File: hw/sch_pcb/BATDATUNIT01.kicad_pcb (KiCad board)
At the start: 2 copper layers, 136.2 x 85.9 mm, 221 parts, among them J1 USBC_USB4105-GF-A, J2 SD_Card-FPS009-4200-0, J3 HEADER_2x03, J4 46436-9327, Q1 BC817-25, Q2 BC817-25, Q3 BC817-25, Q4 BC817-25, Q5 BC817-25, Q6 BC817-25, Q7 BSS83P, SW1 SKRTLAE010, SW2 KMT031, SW3 SKRTLAE010, SW4 KMT031, U1 MAX14502AETL+, U10 PCF85263A, U11 TCA4307, U12 BQ34Z100, U13 BQ25628E, U14 SN74HC164P, U15 TPS631000DRLR, U16 TPS631000DRLR, U17 TPS631000DRLR, U18 TPS22965-Q1, U2 USBLC6-2SC6, U4 PCA9541ABS/01, U5 AT24CS64-SSHM, U6 SHT35-DIS, U7 TMUX1574DYYR, U8 ATMEGA1284P-AU, U9 MS561101BA03-50, Y1 19.2 MHz, Y2 8 MHz, Y3 ABS07-120-32.768KHZ-T

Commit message: Resolve majority of DRC issues.
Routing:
- net GND: track 91.3 -> 94.1 mm, vias 162 -> 163
- net +3.3V: track 564.8 -> 566.3 mm

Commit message: Change oscillator footprint. WIP
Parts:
- Y1: footprint Crystal:Crystal_SMD_2016-4Pin_2.0x1.6mm -> Crystal:Crystal_SMD_2520-4Pin_2.5x2.0mm
- moved R4 0.51 mm to (189.0, 94.5)
- moved R3 0.34 mm to (186.1, 94.7)
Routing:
- net Net-(C49-Pad1): track 7.74 -> 1.91 mm
- net /FREF: track 10.6 -> 10.00 mm
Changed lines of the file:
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@@
   )
   (footprint "Resistor_SMD:R_0805_2012Metric" (layer "B.Cu")
-    (at 188.55 94.3 90)
+    (at 189.0268 94.488 90)
     (descr "Resistor SMD 0805 (2012 Metric), square (rectangular) end terminal, IPC_7351 nominal, (Body size source: IPC-SM-782 page 72, https://www.pcb-3d.com/wordpress/wp-content/uploads/ipc-sm-782a_amendment_1_and_2.pdf), generated with kicad-footprint-generator")
     (tags "resistor")
@@
   )
   (footprint "Resistor_SMD:R_0805_2012Metric" (layer "B.Cu")
-    (at 185.85 94.5 180)
+    (at 186.1058 94.7166 180)
     (descr "Resistor SMD 0805 (2012 Metric), square (rectangular) end terminal, IPC_7351 nominal, (Body size source: IPC-SM-782 page 72, https://www.pcb-3d.com/wordpress/wp-content/uploads/ipc-sm-782a_amendment_1_and_2.pdf), generated with kicad-footprint-generator")
     (tags "resistor")
@@
     )
   )
-  (footprint "Crystal:Crystal_SMD_2016-4Pin_2.0x1.6mm" (layer "B.Cu")
+  (footprint "Crystal:Crystal_SMD_2520-4Pin_2.5x2.0mm" (layer "B.Cu")
     (at 186.1 92.2)
-    (descr "SMD Crystal SERIES SMD2016/4 http://www.q-crystal.com/upload/5/2015552223166229.pdf, 2.0x1.6mm^2 package")
+    (descr "SMD Crystal SERIES SMD2520/4 http://www.newxtal.com/UploadFiles/Images/2012-11-12-09-29-09-776.pdf, 2.5x2.0mm^2 package")
     (tags "SMD SMT crystal")
     (property "Sheetfile" "BATDATUNIT01.kicad_sch")
@@
     (property "ki_keywords" "Crystal Clock Oscillator")
     (attr smd)
-    (fp_text reference "Y1" (at 2.05 -1.35) (layer "B.SilkS")
-        (effects (font (size 0.8 0.8) (thickness 0.1)) (justify mirror))
+    (fp_text reference "Y1" (at 0 2.2 180) (layer "B.SilkS")
+        (effects (font (size 1 1) (thickness 0.15)) (justify mirror))
     )
-    (fp_text value "19.2 MHz" (at 0 -2) (layer "B.Fab")
+    (fp_text value "19.2 MHz" (at 0 -2.2 180) (layer "B.Fab")
         (effects (font (size 1 1) (thickness 0.15)) (justify mirror))
     )
-    (fp_text user "${REFERENCE}" (at 0 0) (layer "B.Fab")
-        (effects (font (size 0.5 0.5) (thickness 0.075)) (justify mirror))
+    (fp_text user "${REFERENCE}" (at 0 0 180) (layer "B.Fab")
+        (effects (font (size 0.6 0.6) (thickness 0.09)) (justify mirror))
     )
-    (fp_line (start -1.35 -1.15) (end 1.35 -1.15)
+    (fp_line (start -1.65 -1.4) (end 1.65 -1.4)
       (stroke (width 0.12) (type solid)) (layer "B.SilkS"))
-    (fp_line (start -1.35 1.15) (end -1.35 -1.15)
+    (fp_line (start -1.65 1.4) (end -1.65 -1.4)
       (stroke (width 0.12) (type solid)) (layer "B.SilkS"))
-    (fp_line (start -1.4 -1.3) (end 1.4 -1.3)
+    (fp_line (start -1.7 -1.5) (end 1.7 -1.5)
       (stroke (width 0.05) (type solid)) (layer "B.CrtYd"))
-    (fp_line (start -1.4 1.3) (end -1.4 -1.3)
+    (fp_line (start -1.7 1.5) (end -1.7 -1.5)
       (stroke (width 0.05) (type solid)) (layer "B.CrtYd"))
-    (fp_line (start 1.4 -1.3) (end 1.4 1.3)
+    (fp_line (start 1.7 -1.5) (end 1.7 1.5)
       (stroke (width 0.05) (type solid)) (layer "B.CrtYd"))
-    (fp_line (start 1.4 1.3) (end -1.4 1.3)
+    (fp_line (start 1.7 1.5) (end -1.7 1.5)
       (stroke (width 0.05) (type solid)) (layer "B.CrtYd"))
-    (fp_line (start -1 -0.7) (end -1 0.7)
+    (fp_line (start -1.25 -0.9) (end -1.25 0.9)
       (stroke (width 0.1) (type solid)) (layer "B.Fab"))
-    (fp_line (start -1 -0.3) (end -0.5 -0.8)
+    (fp_line (start -1.25 0) (end -0.25 -1)
       (stroke (width 0.1) (type solid)) (layer "B.Fab"))
-    (fp_line (start -1 0.7) (end -0.9 0.8)
+    (fp_line (start -1.25 0.9) (end -1.15 1)
       (stroke (width 0.1) (type solid)) (layer "B.Fab"))
-    (fp_line (start -0.9 -0.8) (end -1 -0.7)
+    (fp_line (start -1.15 -1) (end -1.25 -0.9)
       (stroke (width 0.1) (type solid)) (layer "B.Fab"))
-    (fp_line (start -0.9 0.8) (end 0.9 0.8)
+    (fp_line (start -1.15 1) (end 1.15 1)
       (stroke (width 0.1) (type solid)) (layer "B.Fab"))
-    (fp_line (start 0.9 -0.8) (end -0.9 -0.8)
+    (fp_line (start 1.15 -1) (end -1.15 -1)
       (stroke (width 0.1) (type solid)) (layer "B.Fab"))
-    (fp_line (start 0.9 0.8) (end 1 0.7)
+    (fp_line (start 1.15 1) (end 1.25 0.9)
       (stroke (width 0.1) (type solid)) (layer "B.Fab"))
-    (fp_line (start 1 -0.7) (end 0.9 -0.8)
+    (fp_line (start 1.25 -0.9) (end 1.15 -1)
       (stroke (width 0.1) (type solid)) (layer "B.Fab"))
-    (fp_line (start 1 0.7) (end 1 -0.7)
+    (fp_line (start 1.25 0.9) (end 1.25 -0.9)
       (stroke (width 0.1) (type solid)) (layer "B.Fab"))
-    (pad "1" smd rect (at -0.7 -0.55) (size 0.9 0.8) (layers "B.Cu" "B.Paste" "B.Mask")
+    (pad "1" smd rect (at -0.875 -0.7) (size 1.15 1) (layers "B.Cu" "B.Paste" "B.Mask")
       (net 212 "/mode_osc") (pinfunction "EN") (pintype "input"))
-    (pad "2" smd rect (at 0.7 -0.55) (size 0.9 0.8) (layers "B.Cu" "B.Paste" "B.Mask")
+    (pad "2" smd rect (at 0.875 -0.7) (size 1.15 1) (layers "B.Cu" "B.Paste" "B.Mask")
       (net 1 "GND") (pinfunction "GND") (pintype "power_in"))
-    (pad "3" smd rect (at 0.7 0.55) (size 0.9 0.8) (layers "B.Cu" "B.Paste" "B.Mask")
+    (pad "3" smd rect (at 0.875 0.7) (size 1.15 1) (layers "B.Cu" "B.Paste" "B.Mask")
       (net 165 "Net-(Y1-OUT)") (pinfunction "OUT") (pintype "output"))
-    (pad "4" smd rect (at -0.7 0.55) (size 0.9 0.8) (layers "B.Cu" "B.Paste" "B.Mask")
+    (pad "4" smd rect (at -0.875 0.7) (size 1.15 1) (layers "B.Cu" "B.Paste" "B.Mask")
       (net 89 "+3.3V") (pinfunction "VDD") (pintype "power_in"))
-    (model "${KICAD7_3DMODEL_DIR}/Crystal.3dshapes/Crystal_SMD_MicroCrystal_CC8V-T1A-2Pin_2.0x1.2mm.step"
+    (model "${KICAD6_3DMODEL_DIR}/Crystal.3dshapes/Crystal_SMD_2520-4Pin_2.5x2.0mm.wrl"
       (offset (xyz 0 0 0))
       (scale (xyz 1 1 1))
@@
   (segment (start 186.8 93.2) (end 186.8 94.9625) (width 0.4) (layer "B.Cu") (net 165))
   (segment (start 186.8 94.9625) (end 186.7625 95) (width 0.4) (layer "B.Cu") (net 165))
-  (segment (start 178.9 99) (end 178.9 94.6505) (width 0.3) (layer "F.Cu") (net 166))
-  (segment (start 178.601527 99.298473) (end 178.9 99) (width 0.3) (layer "F.Cu") (net 166))
-  (segment (start 178.9 94.6505) (end 178.9005 94.65) (width 0.3) (layer "F.Cu") (net 166))
-  (segment (start 178.3255 99.298473) (end 178.601527 99.298473) (width 0.3) (layer "F.Cu") (net 166))
-  (via (at 178.9005 94.65) (size 0.5) (drill 0.3) (layers "F.Cu" "B.Cu") (net 166))
+  (segment (start 178.9 95.0976) (end 178.9 99) (width 0.3) (layer "F.Cu") (net 166))
+  (segment (start 178.601527 99.298473) (end 178.3255 99.298473) (width 0.3) (layer "F.Cu") (net 166))
+  (segment (start 178.9 99) (end 178.601527 99.298473) (width 0.3) (layer "F.Cu") (net 166))
+  (via (at 178.9 95.0976) (size 0.5) (drill 0.3) (layers "F.Cu" "B.Cu") (net 166))
   (via (at 178.3255 99.298473) (size 0.5) (drill 0.3) (layers "F.Cu" "B.Cu") (net 166))
   (segment (start 176.581371 99.25) (end 175.35 99.25) (width 0.2) (layer "B.Cu") (net 166))
   (segment (start 178.3255 99.298473) (end 178.024173 99.5998) (width 0.2) (layer "B.Cu") (net 166))
+  (segment (start 181.0476 95.0976) (end 181.05 95.1) (width 0.3) (layer "B.Cu") (net 166))
   (segment (start 178.024173 99.5998) (end 176.931172 99.5998) (width 0.2) (layer "B.Cu") (net 166))
   (segment (start 176.931172 99.5998) (end 176.581371 99.25) (width 0.2) (layer "B.Cu") (net 166))
-  (segment (start 178.9005 94.65) (end 180.6 94.65) (width 0.3) (layer "B.Cu") (net 166))
-  (segment (start 180.6 94.65) (end 181.05 95.1) (width 0.3) (layer "B.Cu") (net 166))
+  (segment (start 178.9 95.0976) (end 181.0476 95.0976) (width 0.3) (layer "B.Cu") (net 166))
   (segment (start 125.53 123.77) (end 125.5 123.8) (width 0.3) (layer "F.Cu") (net 167))
   (segment (start 126.590661 123.77) (end 125.53 123.77) (width 0.3) (layer "F.Cu") (net 167))
@@
   (segment (start 168.8 79.95) (end 168.8 79) (width 0.3) (layer "B.Cu") (net 216))
   (segment (start 168.799739 79.950261) (end 168.8 79.95) (width 0.3) (layer "B.Cu") (net 216))
-  (segment (start 184.9375 94.55) (end 184.9375 95.5875) (width 0.4) (layer "B.Cu") (net 217))
-  (segment (start 185 95.65) (end 182.95 95.65) (width 0.4) (layer "B.Cu") (net 217))
+  (segment (start 189.0268 95.4005) (end 188.2995 95.4005) (width 0.4) (layer "B.Cu") (net 217))
   (segment (start 183.15 94.9) (end 182.95 95.1) (width 0.4) (layer "B.Cu") (net 217))
-  (segment (start 188.55 95.2125) (end 188.4875 95.2125) (width 0.4) (layer "B.Cu") (net 217))
-  (segment (start 188.4875 95.2125) (end 188.05 95.65) (width 0.4) (layer "B.Cu") (net 217))
-  (segment (start 188.05 95.65) (end 185 95.65) (width 0.4) (layer "B.Cu") (net 217))
-  (segment (start 184.9375 95.5875) (end 185 95.65) (width 0.4) (layer "B.Cu") (net 217))
   (segment (start 182.95 95.65) (end 182.95 95.1) (width 0.4) (layer "B.Cu") (net 217))
+  (segment (start 188.2995 95.4005) (end 188.05 95.65) (width 0.4) (layer "B.Cu") (net 217))
   (zone (net 14) (net_name "+BATT") (layer "F.Cu") (name "BAT+") (hatch edge 0.5)
     (priority 5)

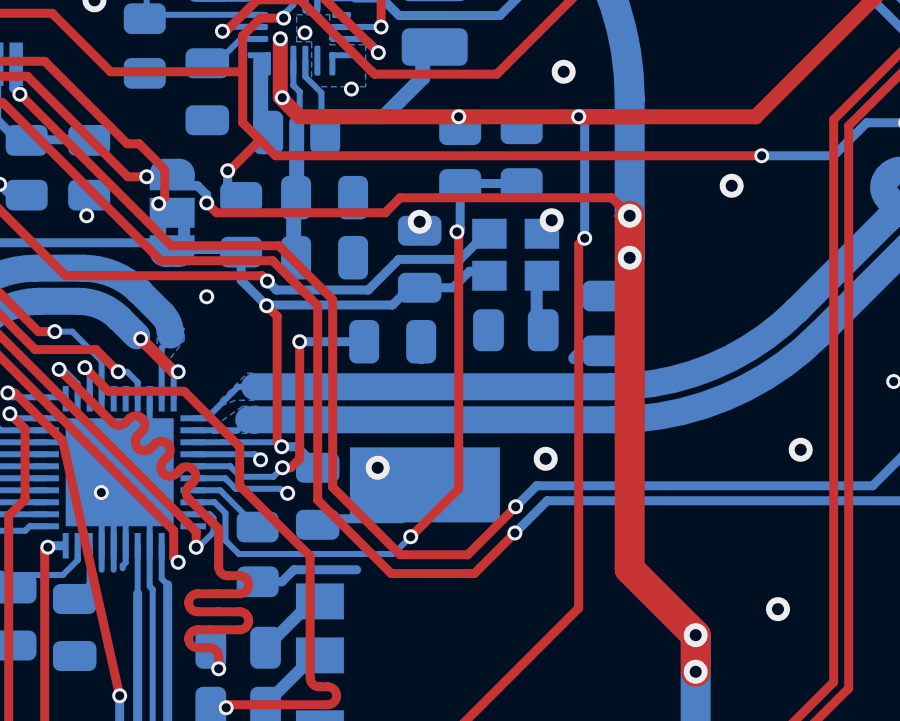
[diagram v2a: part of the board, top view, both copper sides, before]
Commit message: Routed Oscillator in 2.5x2 mm package.
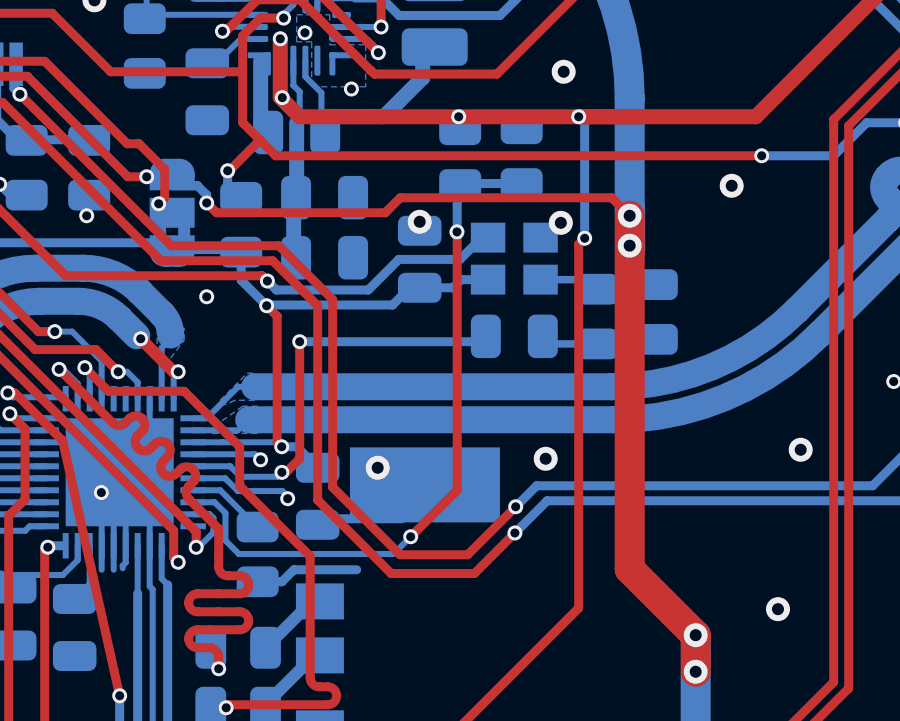
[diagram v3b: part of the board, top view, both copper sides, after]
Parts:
- moved C49 4.06 mm to (186.1, 94.9)
- moved R3 2.76 mm to (188.8, 94.3), turned to -90 degrees
- moved R4 1.82 mm to (190.8, 94.1)
- moved Y1 0.14 mm to (186.1, 92.3)
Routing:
- net /FREF: track 10.00 -> 14.1 mm
- net Net-(C49-Pad1): track 1.91 -> 3.97 mm

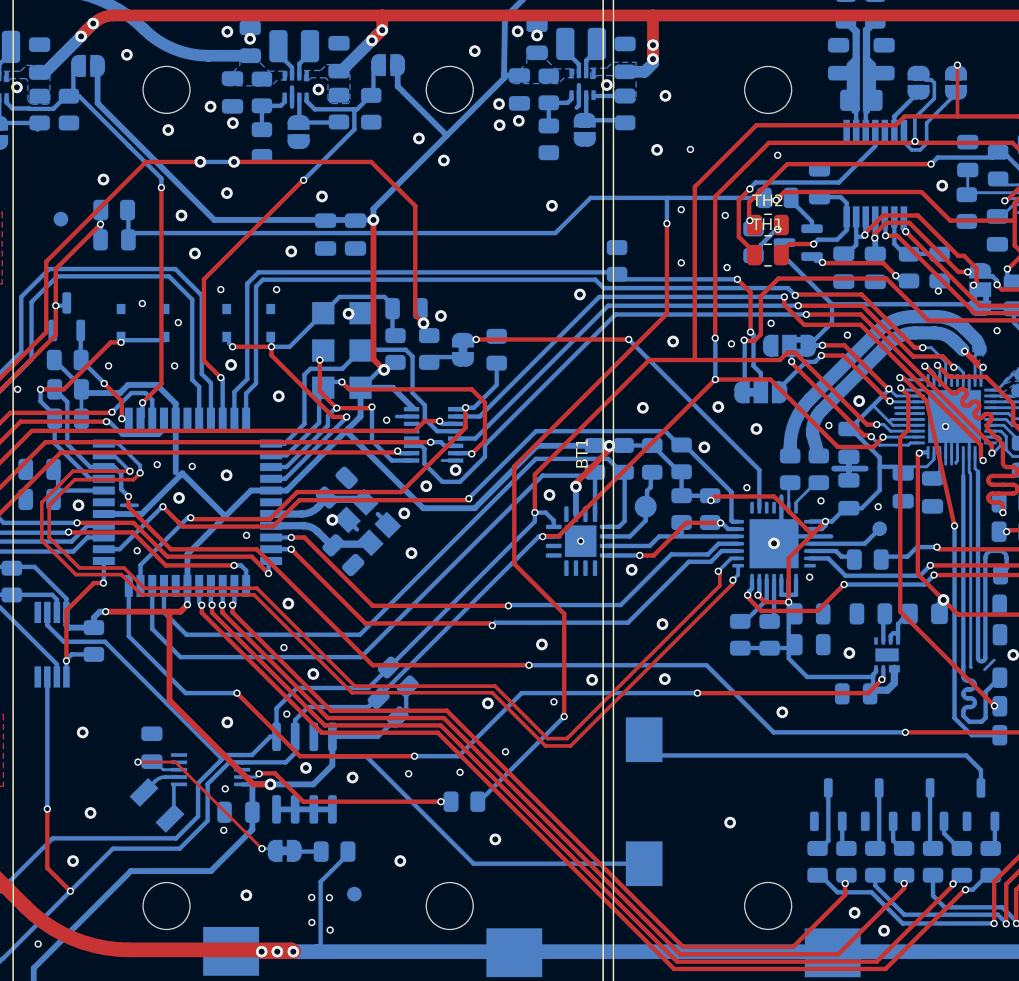
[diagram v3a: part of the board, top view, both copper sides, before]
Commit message: Add blocking capacitor to EEPROM.
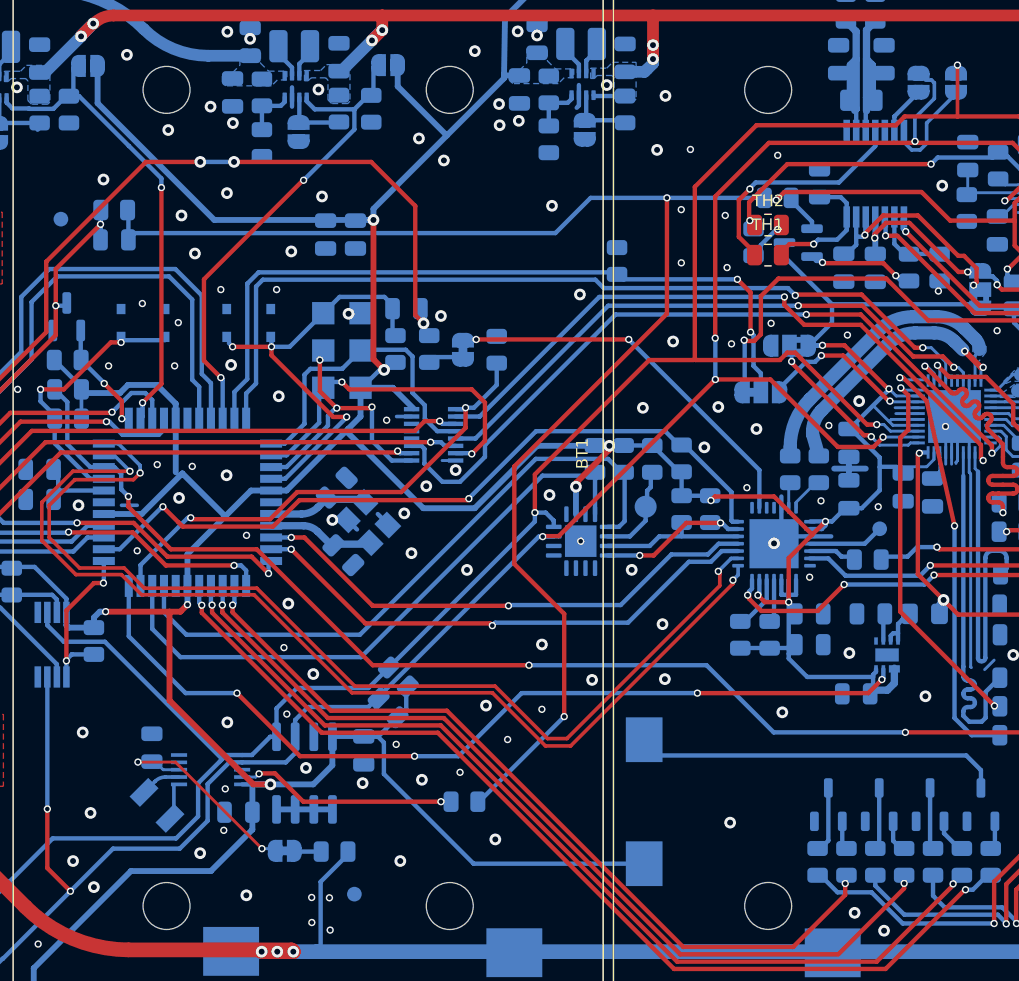
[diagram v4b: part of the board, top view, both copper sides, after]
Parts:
- added C50: 100n, Capacitor_SMD:C_0805_2012Metric, B.Cu at (132.6, 122.2)
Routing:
- net +3.3V: track 565.9 -> 564.6 mm
- net GND: vias 163 -> 168

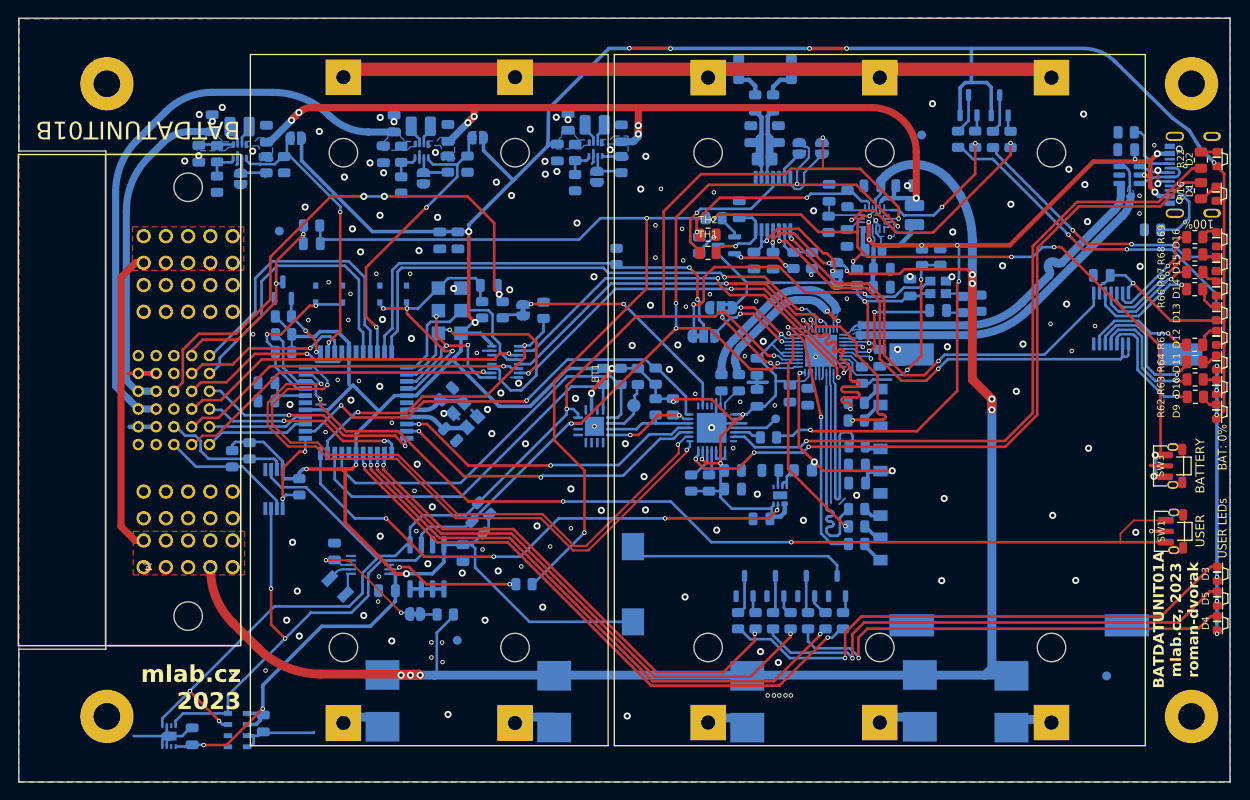
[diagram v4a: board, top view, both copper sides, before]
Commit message: Updata littlefuse footprint to NANO02 fuse holder.
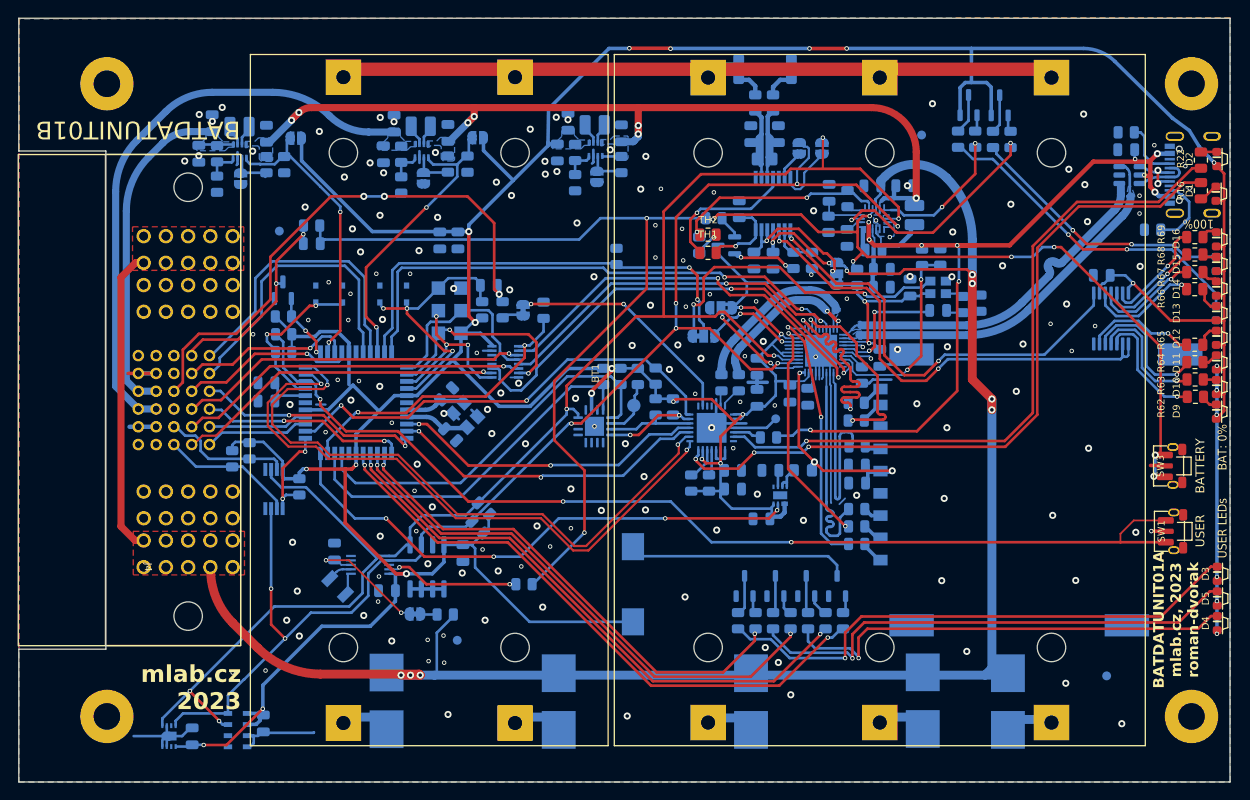
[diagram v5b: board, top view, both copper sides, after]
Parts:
- F1, F2, F3, F4, F5: footprint Mlab_F:Drzak_2410 -> Fuse:Fuseholder_Littelfuse_Nano2_154x
- moved F2 0.51 mm to (143.4, 138.9)
- moved F1 0.45 mm to (124.1, 138.8)
- moved F3 0.42 mm to (165.0, 138.9)
- moved F5 0.40 mm to (193.9, 138.9)
- moved F4 0.33 mm to (184.3, 138.8)
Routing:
- net GND: vias 168 -> 169
